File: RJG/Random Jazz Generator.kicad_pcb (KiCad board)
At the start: 2 copper layers, 109 parts, among them J101 EuroPower, J102 CV, J103 RND, J104 Gate, J105 Trig1, J106 Trig2, J107 Clock, J108 Trig3, J109 Trig4, Q101 BC557, Q102 BC547, Q201 BC547, Q202 BC547, Q401 BC547, Q402 BC547, SW101 Reset, SW301 Reload, SW401 Duration Length, SW402 Reload, U101 L7805, U102 4520, U103 TL082, U201 74LS04, U202 74LS595, U301 74HCT4051, U302 74HCT40105, U303 74LS157, U304 74LS157, U401 4520, U402 74LS74, U403 74LS85, U404 74LS157, U405 SST39SF010, U407 74LS173

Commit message: Finsihed layout
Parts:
- removed the H103 at (194.7, 209.3)
- added C106: 100n, Capacitor_THT:C_Disc_D7.0mm_W2.5mm_P5.00mm, F.Cu at (141.4, 154.5)
- added C107: 100n, Capacitor_THT:C_Disc_D7.0mm_W2.5mm_P5.00mm, F.Cu at (160.4, 140.1)
- added H103 (x2): Mounting_Holes, Kosmo_panel:Kosmo_Panel_Dual_Mounting_Holes, F.Cu at (176.5, 209.3)
- D501, D502, D503, D504, R505, R506, R507, R508: moved to B.Cu
- U101: footprint Package_TO_SOT_THT:TO-220-3_Vertical -> Package_TO_SOT_THT:TO-220-3_Horizontal_TabDown
- moved R501 133.7 mm to (25.7, 183.1)
- moved J105 128.0 mm to (32.0, 196.0)
- moved D501 127.0 mm to (44.4, 188.2), turned to 180 degrees
- moved R110 125.5 mm to (148.4, 175.6), turned to 235 degrees
- moved J107 123.9 mm to (159.9, 186.0), turned to 225 degrees
- moved Q102 123.4 mm to (148.9, 170.0), turned to 0 degrees
- moved R505 120.5 mm to (40.8, 186.7), turned to 270 degrees
- moved J103 119.8 mm to (169.0, 90.1), turned to 270 degrees
- moved R108 118.0 mm to (143.2, 166.1), turned to 115 degrees
- moved C501 116.1 mm to (40.8, 182.7), turned to 180 degrees
- moved R111 114.5 mm to (141.9, 177.5), turned to 75 degrees
- moved R109 111.5 mm to (145.4, 157.8), turned to 303 degrees
- moved RV302 110.5 mm to (133.1, 119.2)
- moved Q101 105.3 mm to (139.3, 170.8), turned to 135 degrees
- moved RV306 103.3 mm to (36.3, 59.9)
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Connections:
- U103 pad 1: Net-(R105-Pad2) -> Net-(R107-Pad2)
- U103 pad 2: Net-(J102-PadT) -> Net-(J104-PadT)
- U103 pad 3: /Notes/CV -> /Notes/Clk
- U103 pad 5: /Notes/Clk -> /Notes/CV
- U103 pad 6: Net-(J104-PadT) -> Net-(J102-PadT)
- U103 pad 7: Net-(R107-Pad2) -> Net-(R105-Pad2)
- U304 pad 4: Net-(U301-Pad11) -> Net-(U301-Pad9)
- U304 pad 9: Net-(U301-Pad9) -> Net-(U301-Pad11)
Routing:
- net +12V: track 0.00 -> 454.8 mm
- net -12V: track 0.00 -> 291.3 mm
- net Net-(C501-Pad1): track 0.00 -> 104.8 mm
- net +5V: track 173.5 -> 76.8 mm
- net /Notes/CV1: track 0.00 -> 91.3 mm
- net /Notes/CV: track 0.00 -> 88.7 mm
- net /Notes/RND: track 0.00 -> 87.1 mm
- net Net-(C502-Pad1): track 0.00 -> 77.1 mm
- net /Notes/CV6: track 0.00 -> 75.4 mm
- net GND: track 218.6 -> 155.2 mm
- net /Notes/CV5: track 0.00 -> 56.5 mm
- net /Notes/CV2: track 0.00 -> 54.6 mm
- net Net-(C503-Pad2): track 0.00 -> 50.3 mm
- net /Notes/Reload: track 0.00 -> 46.1 mm
- net Net-(U301-Pad11): track 15.4 -> 61.2 mm
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- added copper zone on F.Cu, net +5V
- added copper zone on B.Cu, net GND
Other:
- board outline added: 167.8 x 200.6 mm

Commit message: PCB art!
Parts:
- removed the H103 at (176.5, 209.3) (x2)
- added G***: telec-32, logo:telec-32, F.Cu at (31.2, 160.7)
- added H103: Mounting_Holes, Kosmo_panel:Kosmo_Panel_Dual_Mounting_Holes, F.Cu at (176.5, 209.3)
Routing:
- net +5V: track 76.8 -> 97.4 mm, vias 0 -> 7
- net Net-(J103-PadT): track 0.00 -> 2.51 mm
- net Net-(C203-Pad2): track 7.23 -> 9.47 mm
- net +12V: track 454.8 -> 456.3 mm

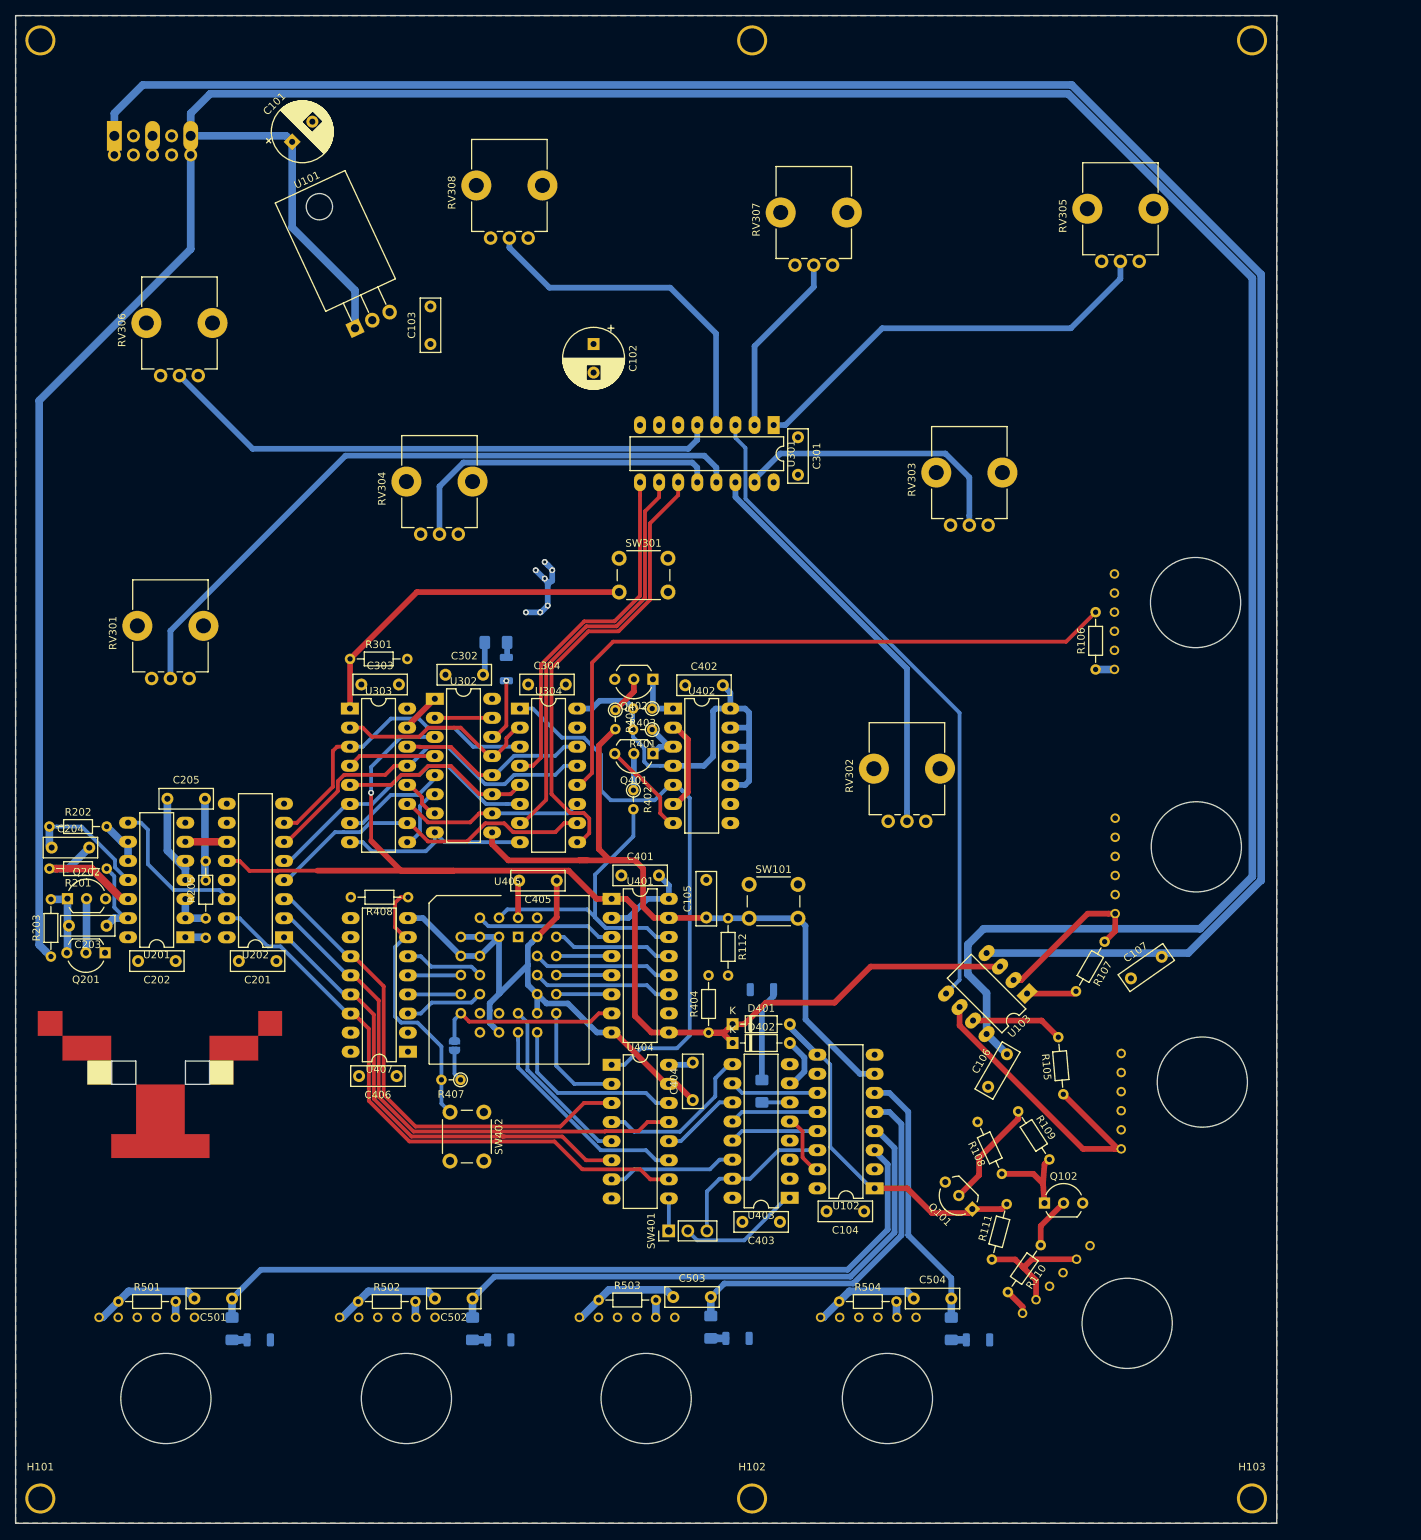
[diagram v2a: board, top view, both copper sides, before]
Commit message: Cleaner schematic, Better Layout
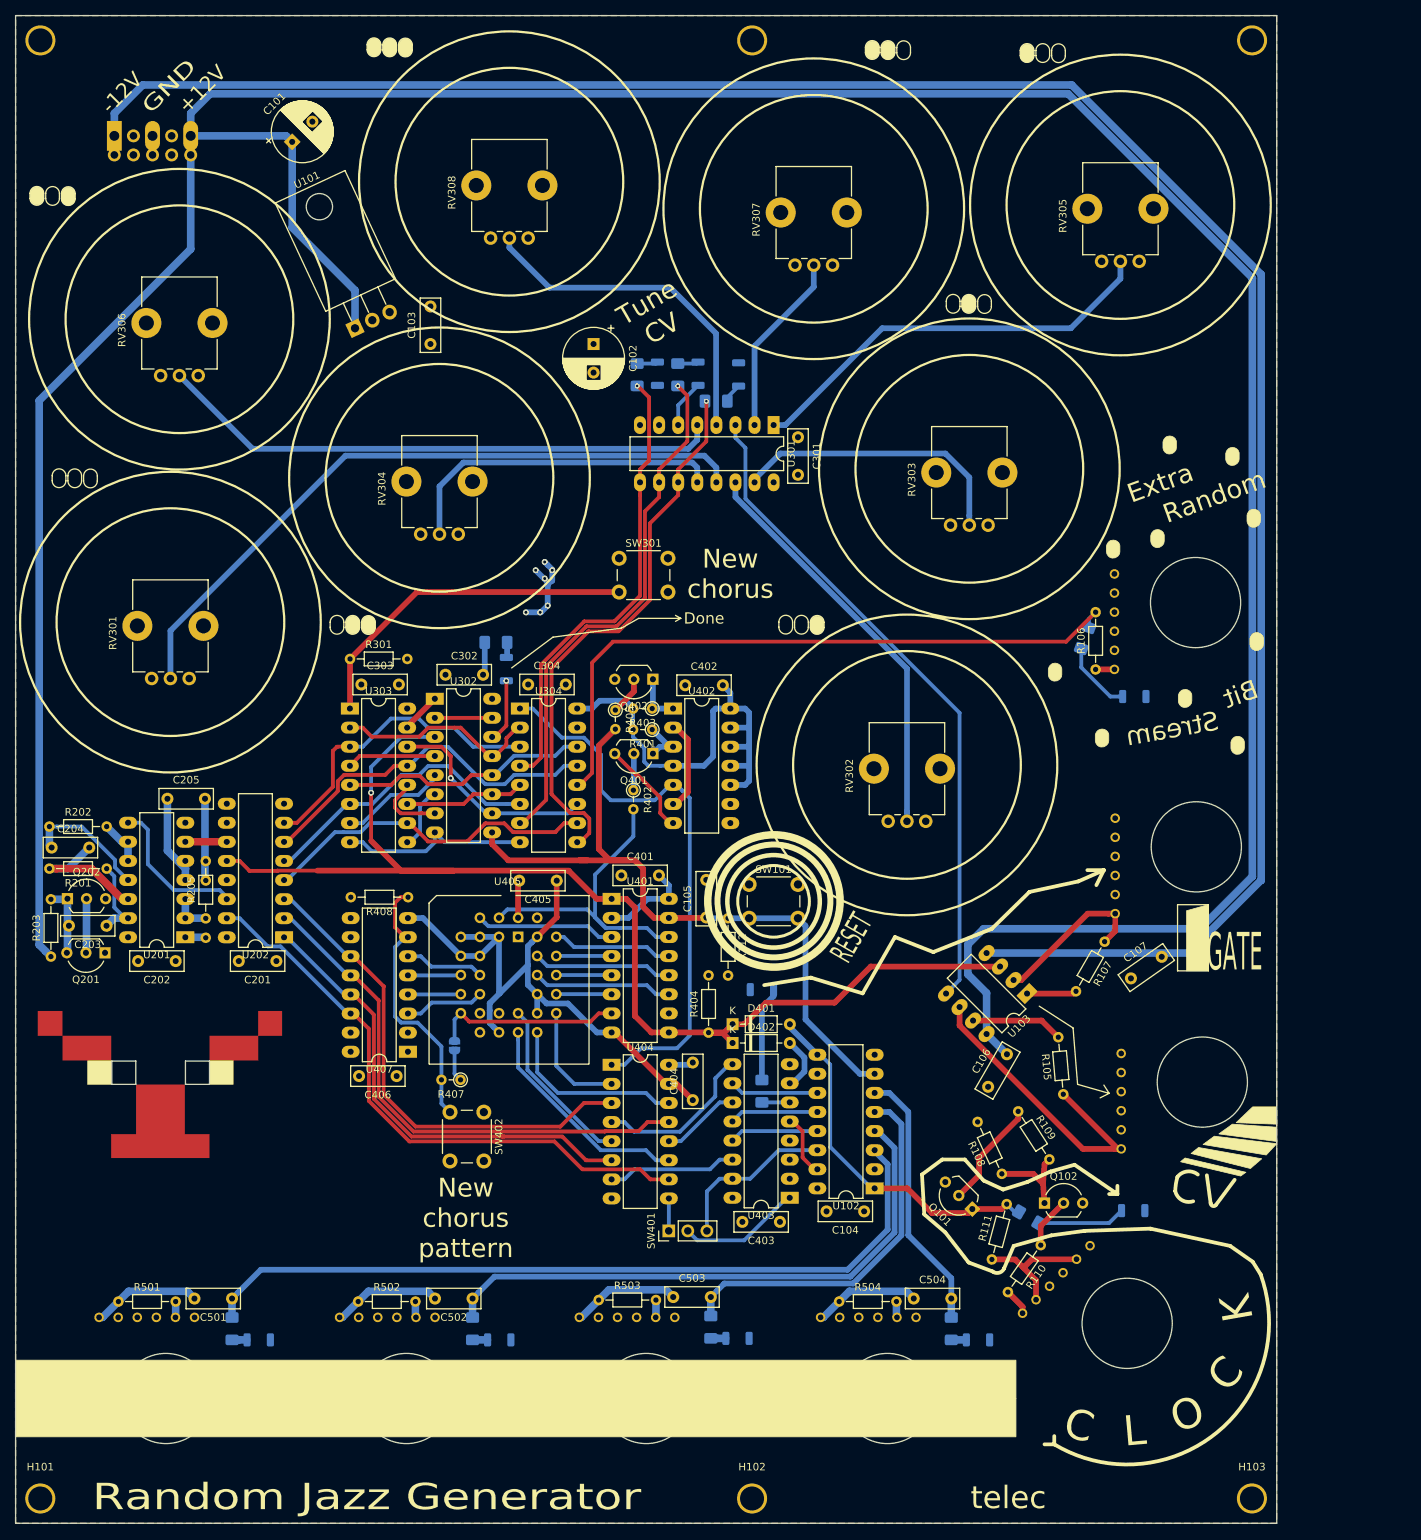
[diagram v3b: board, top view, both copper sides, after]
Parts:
- removed G***: telec-32, logo:telec-32
- added D101: LED, LED_SMD:LED_1206_3216Metric_ReverseMount_Hole1.8x2.4mm, B.Cu at (160.7, 171.0)
- added D302: LED, LED_SMD:LED_1206_3216Metric_ReverseMount_Hole1.8x2.4mm, B.Cu at (108.2, 59.8)
- added D303: LED, LED_SMD:LED_1206_3216Metric_ReverseMount_Hole1.8x2.4mm, B.Cu at (102.8, 59.6)
- added D304: LED, LED_SMD:LED_1206_3216Metric_ReverseMount_Hole1.8x2.4mm, B.Cu at (97.4, 59.6)
- added D305: LED, LED_SMD:LED_1206_3216Metric_ReverseMount_Hole1.8x2.4mm, B.Cu at (160.8, 102.6)
- added LOGO1: telec, logo:telec-32, F.Cu at (31.2, 160.7)
- added R101: 1k, Resistor_SMD:R_1206_3216Metric_Pad1.42x1.75mm_HandSolder, B.Cu at (146.8, 171.9)
- added R303: 1k, Resistor_SMD:R_1206_3216Metric_Pad1.42x1.75mm_HandSolder, B.Cu at (105.2, 63.3)
- added R304: 1k, Resistor_SMD:R_1206_3216Metric_Pad1.42x1.75mm_HandSolder, B.Cu at (100.1, 59.8)
- added R305: 1k, Resistor_SMD:R_1206_3216Metric_Pad1.42x1.75mm_HandSolder, B.Cu at (94.7, 59.8)
- added R306: 1k, Resistor_SMD:R_1206_3216Metric_Pad1.42x1.75mm_HandSolder, B.Cu at (154.3, 94.8)
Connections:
- net /Drums/Clk renamed /Clk
- net /Notes/Clk renamed /Gate
- net Net-(D301-Pad1) renamed /Notes/Full
- net Net-(U301-Pad10) renamed /Notes/S1
- net Net-(U301-Pad11) renamed /Notes/S0
- net Net-(U301-Pad9) renamed /Notes/S2
- U303 pad 11: /Notes/Chorus4 -> /Notes/Chorus3
- U303 pad 14: /Notes/Chorus2 -> /Notes/Chorus4
- U303 pad 5: /Notes/Chorus3 -> /Notes/Chorus2
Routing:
- net /Notes/S1: track 55.6 -> 70.5 mm, vias 0 -> 1
- net /Notes/S2: track 47.7 -> 61.7 mm, vias 0 -> 1
- net /Notes/S0: track 61.2 -> 73.6 mm, vias 0 -> 1
- net Net-(D101-Pad2): track 0.00 -> 11.7 mm
- net Net-(D305-Pad2): track 0.00 -> 9.63 mm
- net /Notes/Chorus3: track 25.7 -> 16.4 mm
- net /Notes/Chorus2: track 25.8 -> 33.3 mm
- net GND: track 155.2 -> 161.6 mm
- net Net-(U302-Pad7): track 5.73 -> 10.0 mm
- net /Notes/Chorus4: track 24.6 -> 28.5 mm, vias 0 -> 1
- net Net-(D304-Pad2): track 0.00 -> 2.78 mm
- net Net-(D303-Pad2): track 0.00 -> 2.78 mm
- net Net-(D302-Pad2): track 0.00 -> 2.62 mm
- net /Notes/RND: track 87.1 -> 89.5 mm
- net /Clk: track 46.4 -> 48.5 mm
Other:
- board text added: "+12V"
- board text added: "-12V"
- board text added: "Bit"
- board text added: "C"
- board text added: "Done"
- board text added: "Drums"
- board text added: "Extra"
- board text added: "GATE"
- board text added: "GND"
- board text added: "IN"
- board text added: "K"
- board text added: "L"
- board text added: "New chorus"
- board text added: "New chorus pattern"
- board text added: "O"
- board text added: "OUT"
- board text added: "RESET"
- board text added: "Random"
- board text added: "Random Jazz Generator"
- board text added: "Stream"
- board text added: "Tune CV"
- board text added: "telec"
